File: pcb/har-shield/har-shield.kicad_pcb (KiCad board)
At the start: 2 copper layers, 60 x 30 mm, 1 part

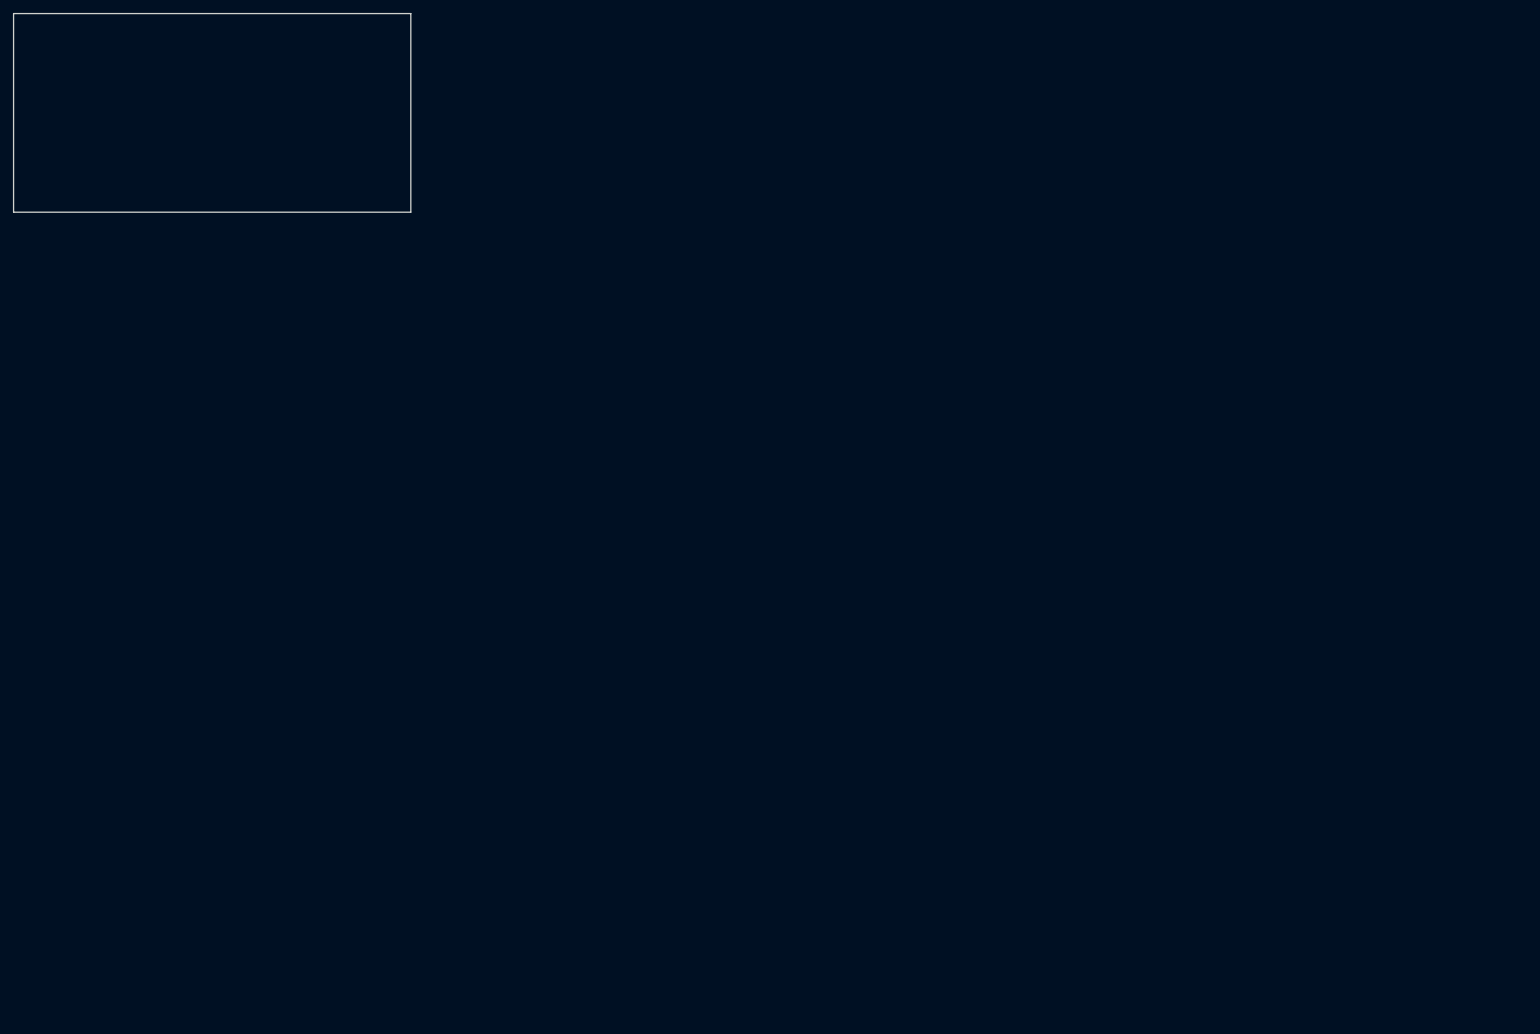
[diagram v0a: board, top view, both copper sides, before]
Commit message: D2: GY-521 six-position calibration + MicroPython firmware
- calib/calibrate.py: six-position accel, ellipsoid mag, Allan variance
- calib/process_mpu6050_calib.py: serial data → calib_params.json + plots
- calib/capture_mpu6050.py: pySerial capture script (bypass Thonny buffer)
- calib/calib_params.json: real GY-521 params (bias/scale/gyro/Allan coeffs)
- firmware/mpu6050_calib/main.py: MicroPython REPL-based calibration firmware
- firmware/har_firmware.ino: Arduino backup (MPU6050+HMC5883L)
- reports/标定报告.md: methods, measured params, Allan noise, comparison charts
- reports/figures/: accel_calib, allan_accel, allan_gyro (real data)
- D2/: delivery package (params + report + figures + raw/calibrated datasets)
- PROJECT_STATUS.md, TODO.md: updated project tracking
- pcb/: user's manual schematic + PCB, gen_sch.py removed
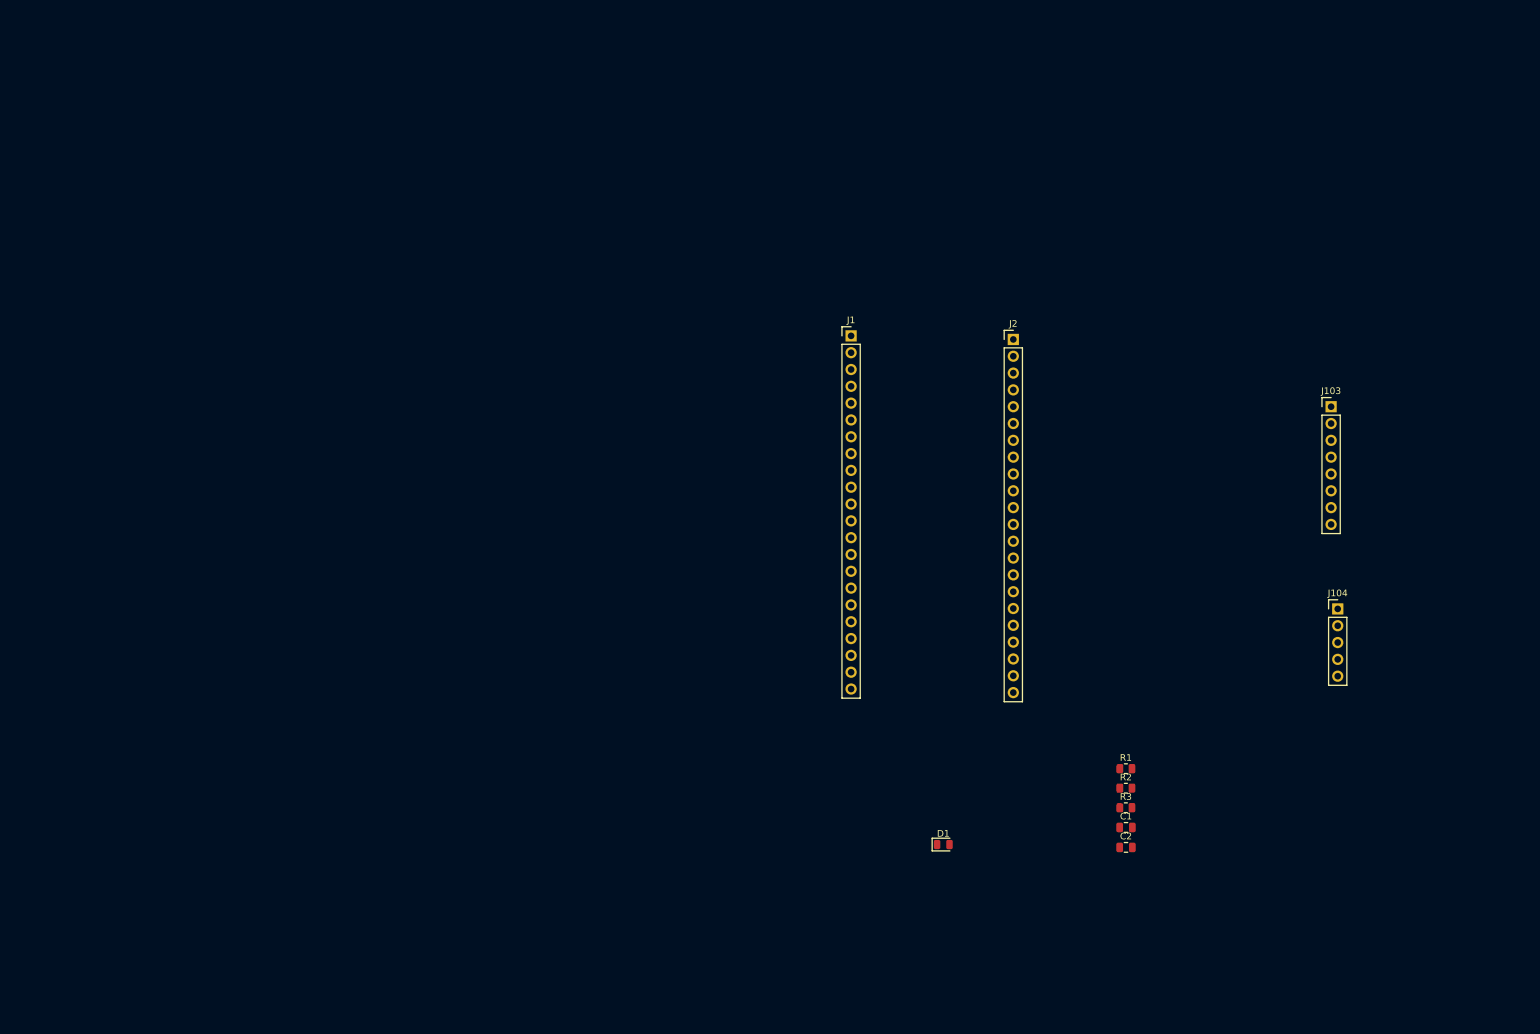
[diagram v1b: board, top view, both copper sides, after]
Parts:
- removed ?: , Board:PCB_60x30mm
- added C1: C, Capacitor_SMD:C_0805_2012Metric, F.Cu at (138.0, 107.9)
- added C2: 100nF, Capacitor_SMD:C_0805_2012Metric, F.Cu at (138.0, 110.9)
- added D1: LED, LED_SMD:LED_0805_2012Metric, F.Cu at (110.4, 110.5)
- added J1: Conn_01x22, Connector_PinHeader_2.54mm:PinHeader_1x22_P2.54mm_Vertical, F.Cu at (96.5, 33.7)
- added J103: Conn_01x08, Connector_PinHeader_2.54mm:PinHeader_1x08_P2.54mm_Vertical, F.Cu at (169.0, 44.4)
- added J104: Conn_01x05, Connector_PinHeader_2.54mm:PinHeader_1x05_P2.54mm_Vertical, F.Cu at (170.0, 74.9)
- added J2: Conn_01x22, Connector_PinHeader_2.54mm:PinHeader_1x22_P2.54mm_Vertical, F.Cu at (121.0, 34.2)
- added R1: R, Resistor_SMD:R_0805_2012Metric, F.Cu at (138.0, 99.0)
- added R2: 4.7k, Resistor_SMD:R_0805_2012Metric, F.Cu at (138.0, 102.0)
- added R3: 220, Resistor_SMD:R_0805_2012Metric, F.Cu at (138.0, 105.0)
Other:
- board outline removed

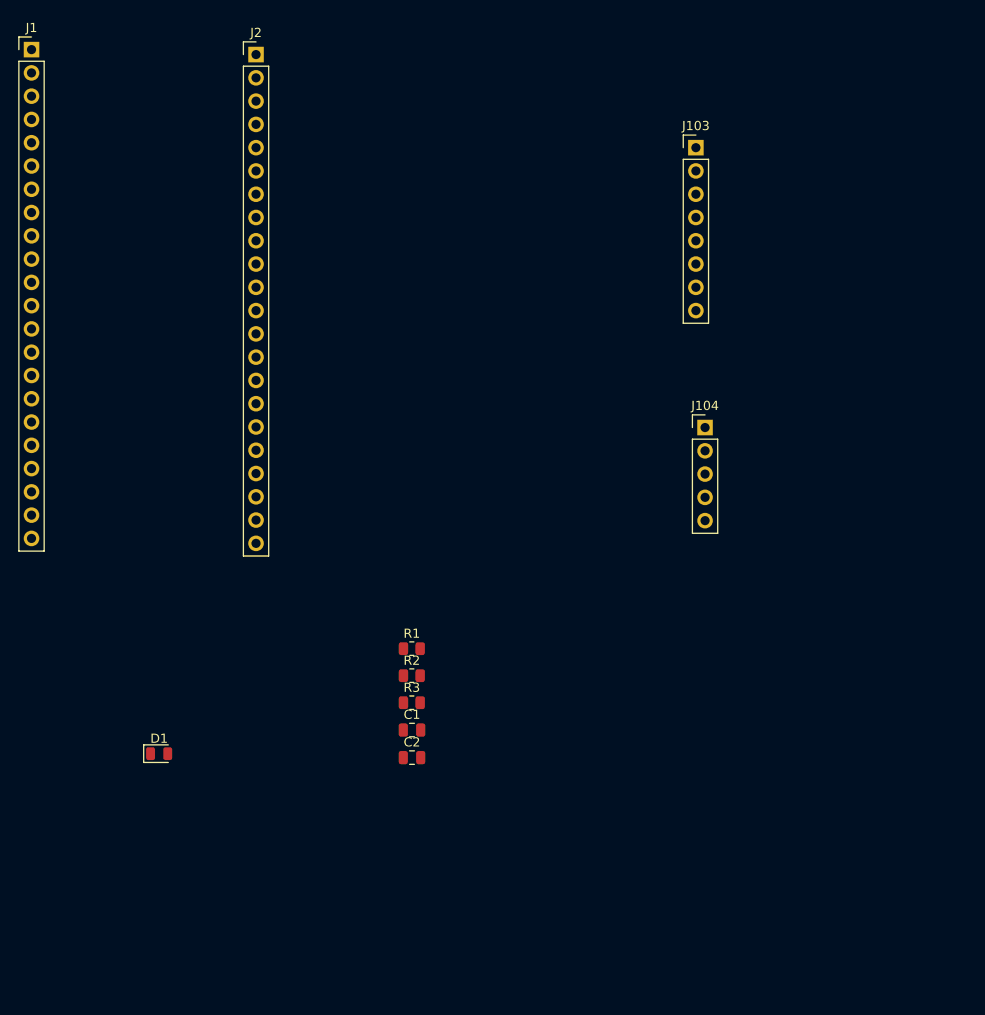
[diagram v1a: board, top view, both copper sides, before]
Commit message: D1-D10: 全链路 HAR 项目完成
## 完成内容
- D1: 项目计划书 + 采集协议 + Git骨架 + KiCad原理图
- D2: 传感器标定 (加速度计六位置 RMSE 11.35→0.42, 磁力计椭球拟合 std 1.22uT)
- D3: 9ch固件 + 预处理Pipeline + 566窗口数据集 (S01+S02 真实数据)
- D4: 294维特征提取 + 特征字典
- D5: 6种特征选择方法 + PCA/LDA/t-SNE (RFE 30维 CV 91.7%)
- D6: 6基线分类器 + MinimumRiskBayes (跌倒漏检×10)
- D7: 7高级模型 + GridSearchCV + 学习曲线
- D8: LOSO + 混淆矩阵 + McNemar (p<0.0001) + Bootstrap 95%CI
- D9: 时序平滑(MV L=7 acc 59.5%) + 1D-CNN(sit 50%) + KMeans/GMM(ARI 0.364)
- D10: 最终报告(5000字) + 答辩PPT(17页) + Demo脚本 + 一键复现 + 交付文件夹

## 硬件
- Shield PCB 焊接 + I2C验证(0x68/0x1E)
- 离线固件: 连续自动序列 + NeoPixel LED + I2C错误恢复
- 真实数据: S01+S02, 14 CSV, 566窗口

## 最佳模型
kNN (k=3,distance) + MajorityVote L=7: Accuracy 59.5%, walk 100%

Co-authored-by: 孔子瑜 <kkawo>
Co-authored-by: 李宝平 <libaoping>
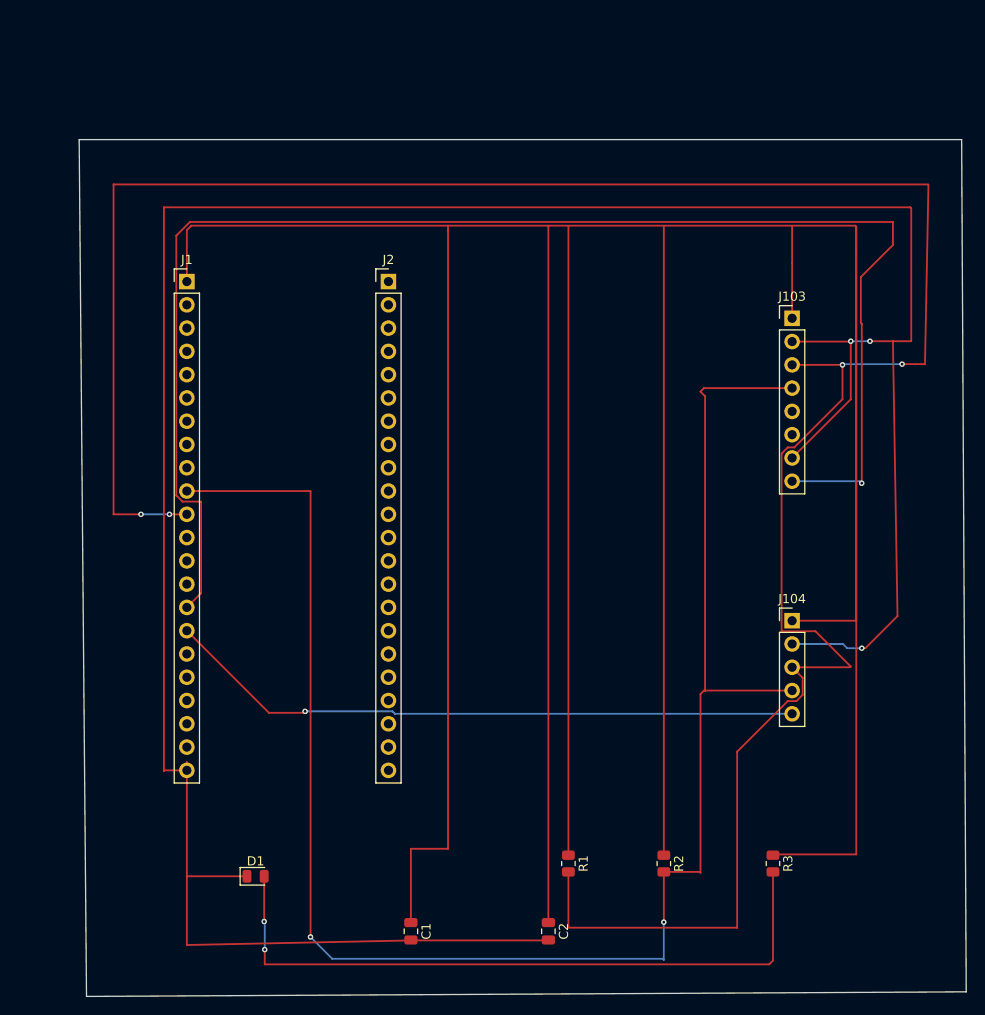
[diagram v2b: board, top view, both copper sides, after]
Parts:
- moved R3 43.1 mm to (177.4, 122.5), turned to -90 degrees
- moved R2 34.3 mm to (165.5, 122.5), turned to -90 degrees
- moved J1 30.5 mm to (113.5, 59.0)
- moved R1 29.0 mm to (155.1, 122.5), turned to -90 degrees
- moved J2 28.7 mm to (135.4, 59.0)
- moved C2 24.1 mm to (152.9, 129.9), turned to -90 degrees
- moved J104 23.1 mm to (179.5, 96.0)
- moved C1 22.0 mm to (137.9, 129.9), turned to -90 degrees
- moved J103 21.4 mm to (179.5, 63.0)
- moved D1 17.0 mm to (121.0, 123.9)
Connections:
- net -3V3 renamed 3V3
- J1 pad 15: unconnected-(J1-Pin_15-Pad15) -> /MPU_INT
- J1 pad 16: unconnected-(J1-Pin_16-Pad16) -> /MAG_DRDY
- J103 pad 8: unconnected-(J103-Pin_8-Pad8) -> /MPU_INT
- J104 pad 5: unconnected-(J104-Pin_5-Pad5) -> /MAG_DRDY
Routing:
- net Net-(D1-K): track 0.00 -> 201.7 mm, vias 0 -> 3
- net Net-(J1-Pin_10): track 0.00 -> 188.0 mm, vias 0 -> 2
- net Net-(J1-Pin_11): track 0.00 -> 163.7 mm, vias 0 -> 4
- net /MPU_INT: track 0.00 -> 160.3 mm, vias 0 -> 1
- net 3V3: track 0.00 -> 84.9 mm
- net Net-(D1-A): track 0.00 -> 75.0 mm, vias 0 -> 2
- net /MAG_DRDY: track 0.00 -> 70.5 mm, vias 0 -> 1
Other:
- board outline added: 96.8 x 93.5 mm
- rule pad_to_mask_clearance: 0.05 -> 0
